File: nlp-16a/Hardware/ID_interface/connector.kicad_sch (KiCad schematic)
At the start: 58 parts, among them J1 Screw_Terminal_01x02, J10 Conn_02x10_Odd_Even, J11 Conn_02x10_Odd_Even, J2 Conn_02x10_Counter_Clockwise, J3 Conn_02x10_Odd_Even, J4 Conn_02x10_Odd_Even, J5 Screw_Terminal_01x02, J6 Screw_Terminal_01x02, J7 Screw_Terminal_01x02, J8 Screw_Terminal_01x02, J9 Conn_02x10_Odd_Even, U10 CD74HC00, U25 CD74HC00, U26 CD74HC00, U27 CD74HC00, U28 CD74HC00

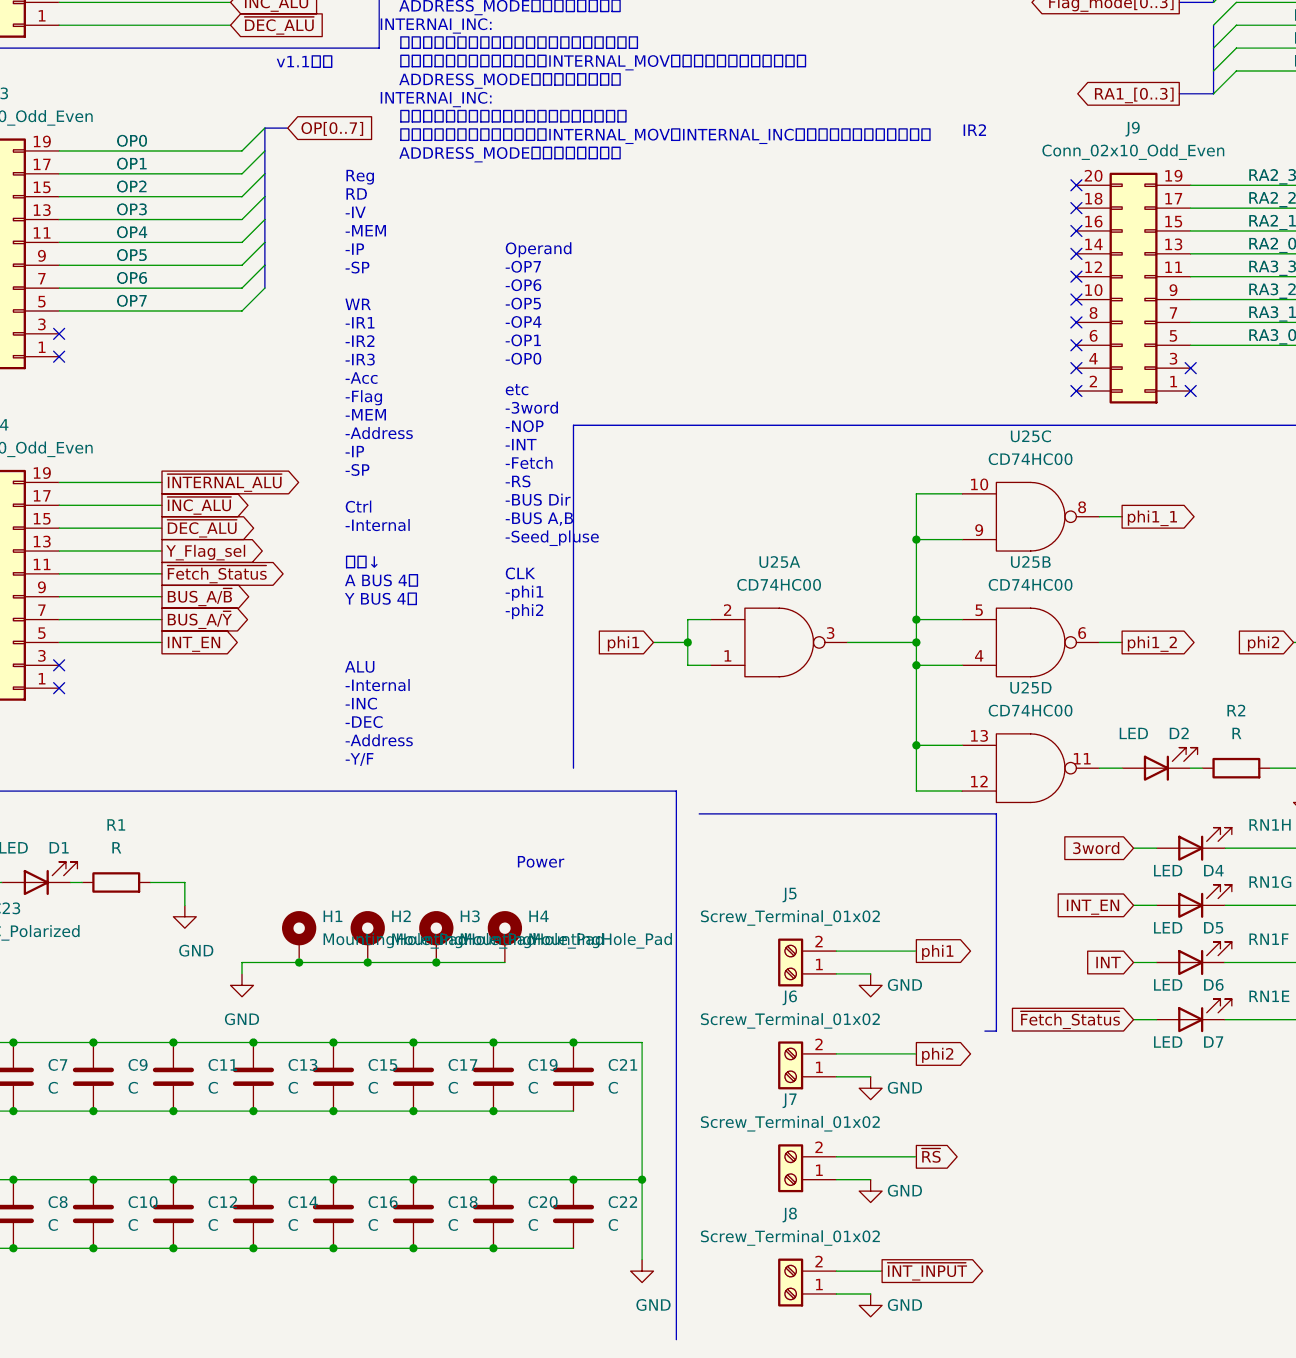
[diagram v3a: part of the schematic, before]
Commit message: v1.1全ガーバーを更新
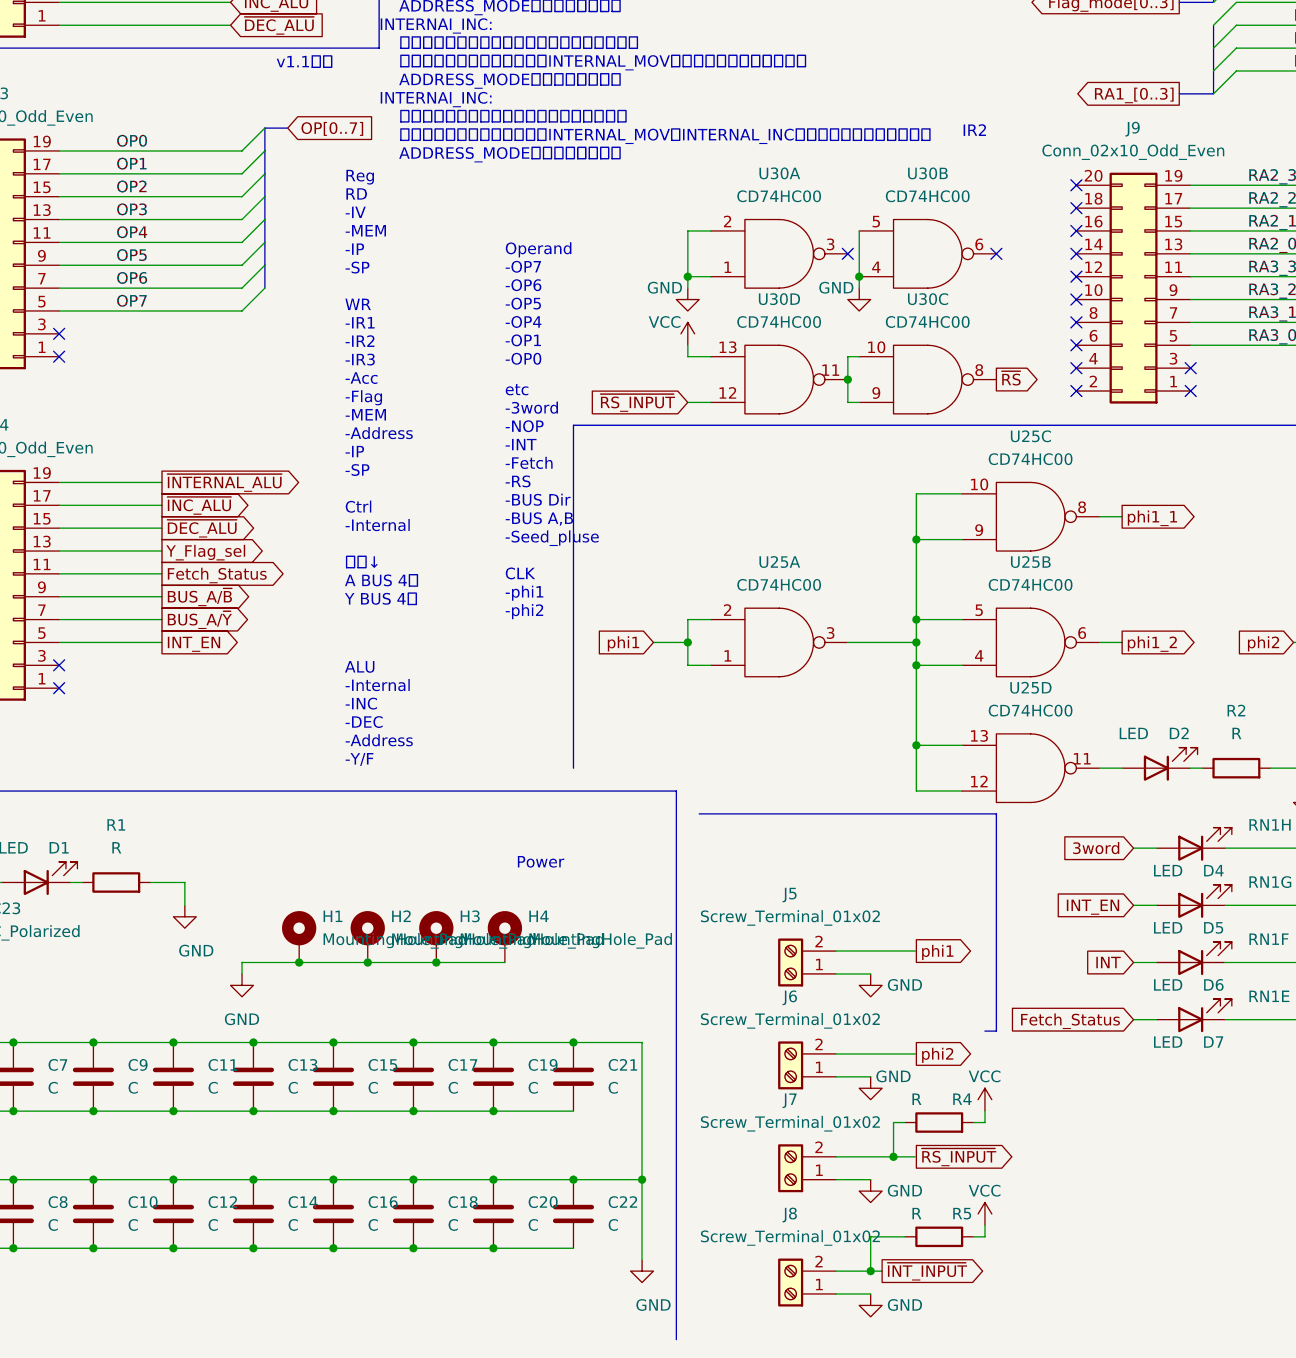
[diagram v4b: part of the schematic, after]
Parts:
- added R4, R5: R, Resistor_SMD:R_0603_1608Metric_Pad0.98x0.95mm_HandSolder, symbol Device:R
- added U30: CD74HC00, Package_DIP:DIP-14_W7.62mm, symbol CD74HCXX:CD74HC00
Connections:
- net GND: now also U30.1, U30.2, U30.4, U30.5, U30.7 (GND), U30.7 (GND), U30.7 (GND), U30.7 (GND)
- net VCC: now also R4.2, R5.2, U30.13, U30.14 (VCC), U30.14 (VCC), U30.14 (VCC), U30.14 (VCC)
- net ~{INT_INPUT}: now also R5.1
- net ~{RS}: now also U30.8; no longer J7.2 (Pin_2)
- net ~{Fetch_Status} renamed Fetch_Status
- new net: U30.10, U30.11, U30.9
- new net ~{RS_INPUT}: J7.2 (Pin_2), R4.1, U30.12
- no-connect marks 61 -> 63
